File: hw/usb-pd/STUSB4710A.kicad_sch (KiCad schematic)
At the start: 13 parts

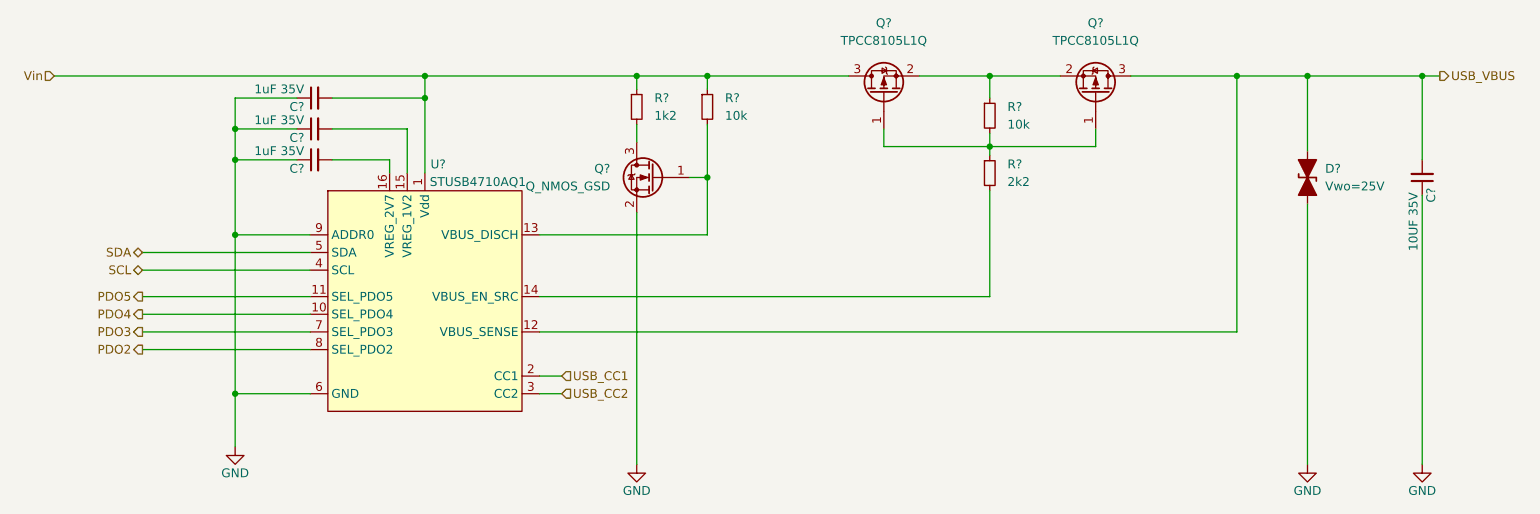
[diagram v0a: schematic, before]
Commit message: Schematic complete, calculation of components required for MAX25240
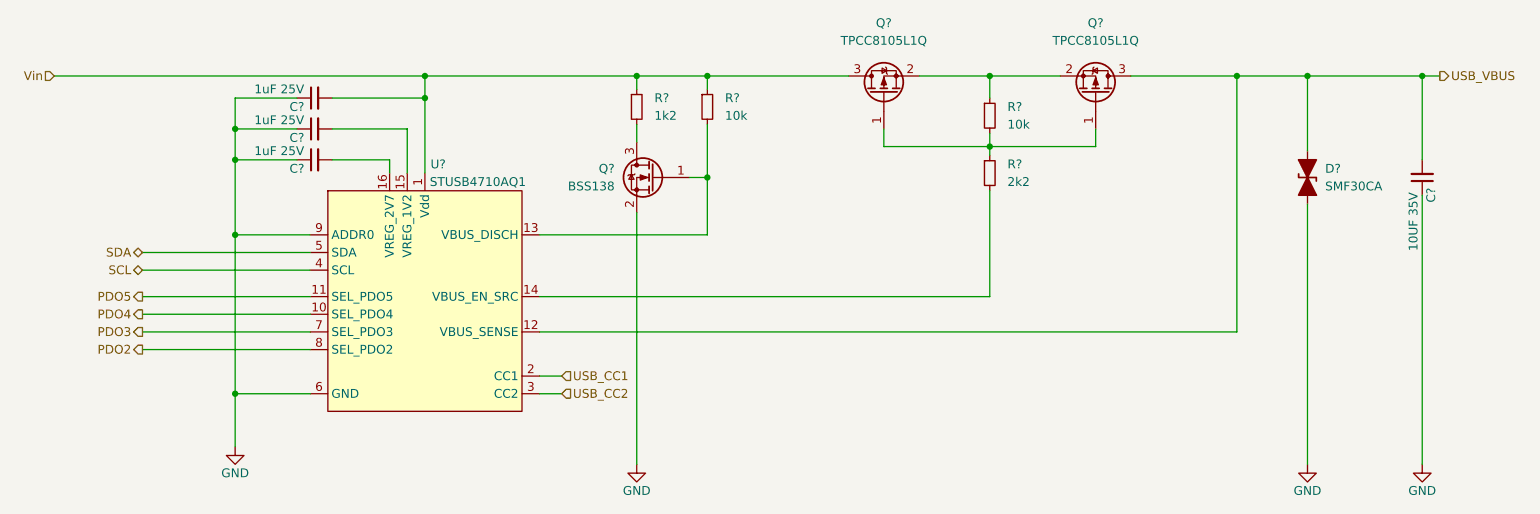
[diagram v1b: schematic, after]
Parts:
- removed Q?: Q_NMOS_GSD, symbol Device:Q_NMOS_GSD
- added Q?: BSS138, Package_TO_SOT_SMD:SOT-23, symbol Transistor_FET:BSS138
- C? (x3): value 1uF 35V -> 1uF 25V; footprint (none) -> Capacitor_SMD:C_0603_1608Metric_Pad1.08x0.95mm_HandSolder
- C?: footprint (none) -> Capacitor_SMD:C_0603_1608Metric_Pad1.08x0.95mm_HandSolder
- D?: value Vwo=25V -> SMF30CA; footprint (none) -> Diode_SMD:D_SOD-123
- Q? (x2): footprint (none) -> footprints:TPCC8105,L1Q
- R? (x4): footprint (none) -> Resistor_SMD:R_0603_1608Metric_Pad0.98x0.95mm_HandSolder
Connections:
- net GND: now also Q?.2 (S)
- net at R?.2: now also Q?.3 (D)
- net at R?.2, U?.13 (VBUS_DISCH): now also Q?.1 (G)
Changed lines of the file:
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@@
       (effects (font (size 1.27 1.27)) (justify left))
     )
-    (property "Footprint" "" (id 2) (at 149.86 61.595 0)
+    (property "Footprint" "Resistor_SMD:R_0603_1608Metric_Pad0.98x0.95mm_HandSolder" (id 2) (at 149.86 61.595 0)
       (effects (font (size 1.27 1.27)) hide)
     )
@@
       (effects (font (size 1.27 1.27)) (justify right))
     )
-    (property "Value" "Vwo=25V" (id 1) (at 248.92 73.0249 90)
+    (property "Value" "SMF30CA" (id 1) (at 248.92 73.0249 90)
       (effects (font (size 1.27 1.27)) (justify right))
     )
-    (property "Footprint" "" (id 2) (at 246.38 71.755 0)
+    (property "Footprint" "Diode_SMD:D_SOD-123" (id 2) (at 246.38 71.755 0)
       (effects (font (size 1.27 1.27)) hide)
     )
@@
     (in_bom yes) (on_board yes)
     (property "Reference" "C?" (id 0) (at 100.965 70.485 90))
-    (property "Value" "1uF 35V" (id 1) (at 98.425 67.945 90))
-    (property "Footprint" "" (id 2) (at 103.505 69.215 0)
+    (property "Value" "1uF 25V" (id 1) (at 98.425 67.945 90))
+    (property "Footprint" "Capacitor_SMD:C_0603_1608Metric_Pad1.08x0.95mm_HandSolder" (id 2) (at 103.505 69.215 0)
       (effects (font (size 1.27 1.27)) hide)
     )
@@
     (property "Reference" "Q?" (id 0) (at 185.42 49.53 90))
     (property "Value" "TPCC8105L1Q" (id 1) (at 185.42 52.07 90))
-    (property "Footprint" "" (id 2) (at 182.88 54.61 0)
+    (property "Footprint" "footprints:TPCC8105,L1Q" (id 2) (at 182.88 54.61 0)
       (effects (font (size 1.27 1.27)) hide)
     )
@@
     (pin "3")
   )
-  (symbol (lib_id "Device:Q_NMOS_GSD") (at 152.4 71.755 0) (mirror y) (unit 1)
-    (in_bom yes) (on_board yes) (fields_autoplaced)
-    (property "Reference" "Q?" (id 0) (at 146.05 70.4849 0)
-      (effects (font (size 1.27 1.27)) (justify left))
-    )
-    (property "Value" "Q_NMOS_GSD" (id 1) (at 146.05 73.0249 0)
-      (effects (font (size 1.27 1.27)) (justify left))
-    )
-    (property "Footprint" "" (id 2) (at 147.32 69.215 0)
-      (effects (font (size 1.27 1.27)) hide)
-    )
-    (property "Datasheet" "~" (id 3) (at 152.4 71.755 0)
-      (effects (font (size 1.27 1.27)) hide)
+  (symbol (lib_id "Transistor_FET:BSS138") (at 152.4 71.755 0) (mirror y) (unit 1)
+    (in_bom yes) (on_board yes) (fields_autoplaced)
+    (property "Reference" "Q?" (id 0) (at 146.685 70.4849 0)
+      (effects (font (size 1.27 1.27)) (justify left))
+    )
+    (property "Value" "BSS138" (id 1) (at 146.685 73.0249 0)
+      (effects (font (size 1.27 1.27)) (justify left))
+    )
+    (property "Footprint" "Package_TO_SOT_SMD:SOT-23" (id 2) (at 147.32 73.66 0)
+      (effects (font (size 1.27 1.27) italic) (justify left) hide)
+    )
+    (property "Datasheet" "https://www.onsemi.com/pub/Collateral/BSS138-D.PDF" (id 3) (at 152.4 71.755 0)
+      (effects (font (size 1.27 1.27)) (justify left) hide)
     )
     (pin "1")
@@
     (property "Reference" "Q?" (id 0) (at 215.9 49.53 90))
     (property "Value" "TPCC8105L1Q" (id 1) (at 215.9 52.07 90))
-    (property "Footprint" "" (id 2) (at 218.44 54.61 0)
+    (property "Footprint" "footprints:TPCC8105,L1Q" (id 2) (at 218.44 54.61 0)
       (effects (font (size 1.27 1.27)) hide)
     )
@@
       (effects (font (size 1.27 1.27)) (justify left))
     )
-    (property "Footprint" "" (id 2) (at 160.02 61.595 0)
+    (property "Footprint" "Resistor_SMD:R_0603_1608Metric_Pad0.98x0.95mm_HandSolder" (id 2) (at 160.02 61.595 0)
       (effects (font (size 1.27 1.27)) hide)
     )
@@
       (effects (font (size 1.27 1.27)) (justify left))
     )
-    (property "Footprint" "" (id 2) (at 200.66 62.865 0)
+    (property "Footprint" "Resistor_SMD:R_0603_1608Metric_Pad0.98x0.95mm_HandSolder" (id 2) (at 200.66 62.865 0)
       (effects (font (size 1.27 1.27)) hide)
     )
@@
     (in_bom yes) (on_board yes)
     (property "Reference" "C?" (id 0) (at 100.965 61.595 90))
-    (property "Value" "1uF 35V" (id 1) (at 98.425 59.055 90))
-    (property "Footprint" "" (id 2) (at 103.505 60.325 0)
+    (property "Value" "1uF 25V" (id 1) (at 98.425 59.055 90))
+    (property "Footprint" "Capacitor_SMD:C_0603_1608Metric_Pad1.08x0.95mm_HandSolder" (id 2) (at 103.505 60.325 0)
       (effects (font (size 1.27 1.27)) hide)
     )
@@
     (property "Reference" "C?" (id 0) (at 264.16 74.295 90))
     (property "Value" "10UF 35V" (id 1) (at 261.62 78.105 90))
-    (property "Footprint" "" (id 2) (at 262.89 71.755 0)
+    (property "Footprint" "Capacitor_SMD:C_0603_1608Metric_Pad1.08x0.95mm_HandSolder" (id 2) (at 262.89 71.755 0)
       (effects (font (size 1.27 1.27)) hide)
     )
@@
       (effects (font (size 1.27 1.27)) (justify left))
     )
-    (property "Footprint" "" (id 2) (at 200.66 71.12 0)
+    (property "Footprint" "Resistor_SMD:R_0603_1608Metric_Pad0.98x0.95mm_HandSolder" (id 2) (at 200.66 71.12 0)
       (effects (font (size 1.27 1.27)) hide)
     )
@@
     (in_bom yes) (on_board yes)
     (property "Reference" "C?" (id 0) (at 100.965 66.04 90))
-    (property "Value" "1uF 35V" (id 1) (at 98.425 63.5 90))
-    (property "Footprint" "" (id 2) (at 103.505 64.77 0)
-      (effects (font (size 1.27 1.27)) hide)
-    )
+    (property "Value" "1uF 25V" (id 1) (at 98.425 63.5 90))
+    (property "Footprint" "Capacitor_SMD:C_0603_1608Metric_Pad1.08x0.95mm_HandSolder" (id 2) (at 103.505 64.77 0)
+      (effects (font (size 1.27 1.27)) hide)
+    )

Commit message: Preliminary PCB layout, calculated compensation filter and feedback network for MAX25240
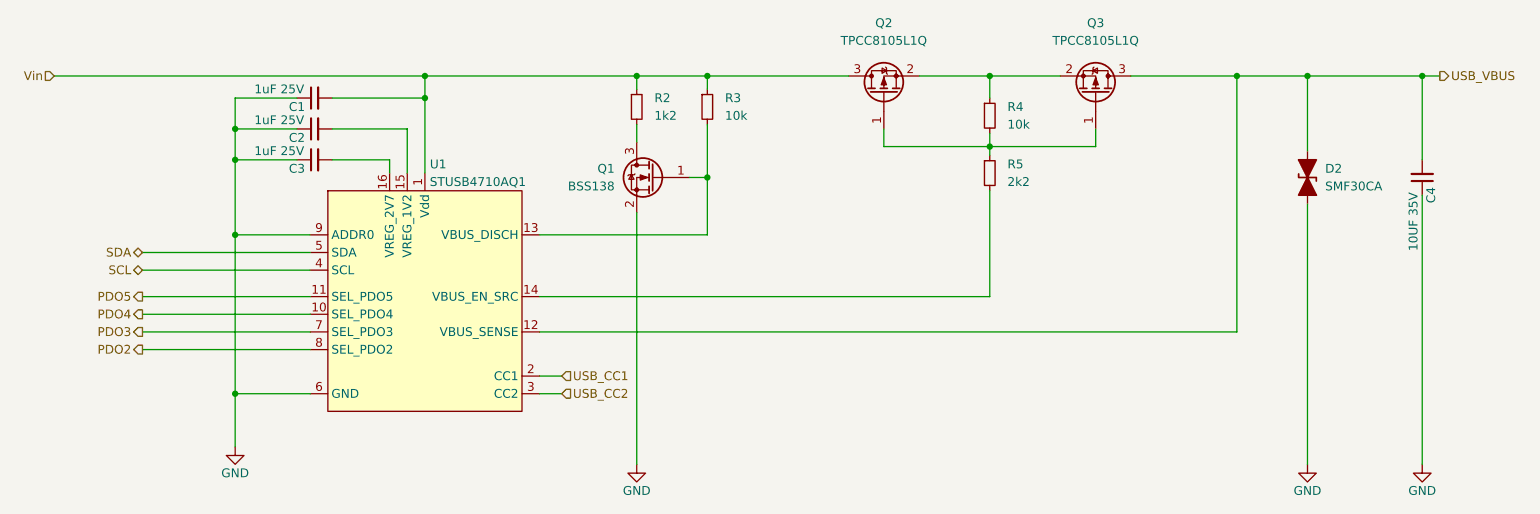
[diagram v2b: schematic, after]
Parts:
- gave numbers to parts that had none: 13
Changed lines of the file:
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@@
   (symbol (lib_id "Device:R_Small") (at 149.86 61.595 0) (unit 1)
     (in_bom yes) (on_board yes) (fields_autoplaced)
-    (property "Reference" "R?" (id 0) (at 152.4 60.3249 0)
+    (property "Reference" "R2" (id 0) (at 152.4 60.3249 0)
       (effects (font (size 1.27 1.27)) (justify left))
     )
@@
   (symbol (lib_id "Device:D_TVS_Filled") (at 246.38 71.755 90) (unit 1)
     (in_bom yes) (on_board yes) (fields_autoplaced)
-    (property "Reference" "D?" (id 0) (at 248.92 70.4849 90)
+    (property "Reference" "D2" (id 0) (at 248.92 70.4849 90)
       (effects (font (size 1.27 1.27)) (justify right))
     )
@@
   (symbol (lib_id "Device:C_Small") (at 103.505 69.215 90) (unit 1)
     (in_bom yes) (on_board yes)
-    (property "Reference" "C?" (id 0) (at 100.965 70.485 90))
+    (property "Reference" "C3" (id 0) (at 100.965 70.485 90))
     (property "Value" "1uF 25V" (id 1) (at 98.425 67.945 90))
     (property "Footprint" "Capacitor_SMD:C_0603_1608Metric_Pad1.08x0.95mm_HandSolder" (id 2) (at 103.505 69.215 0)
@@
   (symbol (lib_id "Device:Q_PMOS_GSD") (at 185.42 59.69 90) (unit 1)
     (in_bom yes) (on_board yes) (fields_autoplaced)
-    (property "Reference" "Q?" (id 0) (at 185.42 49.53 90))
+    (property "Reference" "Q2" (id 0) (at 185.42 49.53 90))
     (property "Value" "TPCC8105L1Q" (id 1) (at 185.42 52.07 90))
     (property "Footprint" "footprints:TPCC8105,L1Q" (id 2) (at 182.88 54.61 0)
@@
   (symbol (lib_id "Transistor_FET:BSS138") (at 152.4 71.755 0) (mirror y) (unit 1)
     (in_bom yes) (on_board yes) (fields_autoplaced)
-    (property "Reference" "Q?" (id 0) (at 146.685 70.4849 0)
+    (property "Reference" "Q1" (id 0) (at 146.685 70.4849 0)
       (effects (font (size 1.27 1.27)) (justify left))
     )
@@
   (symbol (lib_id "Device:Q_PMOS_GSD") (at 215.9 59.69 270) (mirror x) (unit 1)
     (in_bom yes) (on_board yes) (fields_autoplaced)
-    (property "Reference" "Q?" (id 0) (at 215.9 49.53 90))
+    (property "Reference" "Q3" (id 0) (at 215.9 49.53 90))
     (property "Value" "TPCC8105L1Q" (id 1) (at 215.9 52.07 90))
     (property "Footprint" "footprints:TPCC8105,L1Q" (id 2) (at 218.44 54.61 0)
@@
   (symbol (lib_id "symbols:STUSB4710AQ1") (at 119.38 73.66 0) (unit 1)
     (in_bom yes) (on_board yes)
-    (property "Reference" "U?" (id 0) (at 121.285 69.85 0))
+    (property "Reference" "U1" (id 0) (at 121.285 69.85 0))
     (property "Value" "STUSB4710AQ1" (id 1) (at 127 72.39 0))
     (property "Footprint" "footprints:QFN-16-1EP_3x3mm_P0.5mm" (id 2) (at 119.38 62.23 0)
@@
   (symbol (lib_id "power:GND") (at 246.38 113.03 0) (unit 1)
     (in_bom yes) (on_board yes)
-    (property "Reference" "#PWR?" (id 0) (at 246.38 119.38 0)
+    (property "Reference" "#PWR0106" (id 0) (at 246.38 119.38 0)
       (effects (font (size 1.27 1.27)) hide)
     )
@@
   (symbol (lib_id "Device:R_Small") (at 160.02 61.595 0) (unit 1)
     (in_bom yes) (on_board yes) (fields_autoplaced)
-    (property "Reference" "R?" (id 0) (at 162.56 60.3249 0)
+    (property "Reference" "R3" (id 0) (at 162.56 60.3249 0)
       (effects (font (size 1.27 1.27)) (justify left))
     )
@@
   (symbol (lib_id "Device:R_Small") (at 200.66 62.865 0) (unit 1)
     (in_bom yes) (on_board yes) (fields_autoplaced)
-    (property "Reference" "R?" (id 0) (at 203.2 61.5949 0)
+    (property "Reference" "R4" (id 0) (at 203.2 61.5949 0)
       (effects (font (size 1.27 1.27)) (justify left))
     )
@@
   (symbol (lib_id "Device:C_Small") (at 103.505 60.325 90) (unit 1)
     (in_bom yes) (on_board yes)
-    (property "Reference" "C?" (id 0) (at 100.965 61.595 90))
+    (property "Reference" "C1" (id 0) (at 100.965 61.595 90))
     (property "Value" "1uF 25V" (id 1) (at 98.425 59.055 90))
     (property "Footprint" "Capacitor_SMD:C_0603_1608Metric_Pad1.08x0.95mm_HandSolder" (id 2) (at 103.505 60.325 0)
@@
   (symbol (lib_id "power:GND") (at 149.86 113.03 0) (unit 1)
     (in_bom yes) (on_board yes)
-    (property "Reference" "#PWR?" (id 0) (at 149.86 119.38 0)
+    (property "Reference" "#PWR0108" (id 0) (at 149.86 119.38 0)
       (effects (font (size 1.27 1.27)) hide)
     )
@@
   (symbol (lib_id "power:GND") (at 92.075 110.49 0) (unit 1)
     (in_bom yes) (on_board yes)
-    (property "Reference" "#PWR?" (id 0) (at 92.075 116.84 0)
+    (property "Reference" "#PWR0109" (id 0) (at 92.075 116.84 0)
       (effects (font (size 1.27 1.27)) hide)
     )
@@
   (symbol (lib_id "power:GND") (at 262.89 113.03 0) (unit 1)
     (in_bom yes) (on_board yes)
-    (property "Reference" "#PWR?" (id 0) (at 262.89 119.38 0)
+    (property "Reference" "#PWR0107" (id 0) (at 262.89 119.38 0)
       (effects (font (size 1.27 1.27)) hide)
     )
@@
   (symbol (lib_id "Device:C_Small") (at 262.89 71.755 180) (unit 1)
     (in_bom yes) (on_board yes)
-    (property "Reference" "C?" (id 0) (at 264.16 74.295 90))
+    (property "Reference" "C4" (id 0) (at 264.16 74.295 90))
     (property "Value" "10UF 35V" (id 1) (at 261.62 78.105 90))
     (property "Footprint" "Capacitor_SMD:C_0603_1608Metric_Pad1.08x0.95mm_HandSolder" (id 2) (at 262.89 71.755 0)
@@
   (symbol (lib_id "Device:R_Small") (at 200.66 71.12 0) (unit 1)
     (in_bom yes) (on_board yes) (fields_autoplaced)
-    (property "Reference" "R?" (id 0) (at 203.2 69.8499 0)
+    (property "Reference" "R5" (id 0) (at 203.2 69.8499 0)
       (effects (font (size 1.27 1.27)) (justify left))
     )
@@
   (symbol (lib_id "Device:C_Small") (at 103.505 64.77 90) (unit 1)
     (in_bom yes) (on_board yes)
-    (property "Reference" "C?" (id 0) (at 100.965 66.04 90))
+    (property "Reference" "C2" (id 0) (at 100.965 66.04 90))
     (property "Value" "1uF 25V" (id 1) (at 98.425 63.5 90))
     (property "Footprint" "Capacitor_SMD:C_0603_1608Metric_Pad1.08x0.95mm_HandSolder" (id 2) (at 103.505 64.77 0)
